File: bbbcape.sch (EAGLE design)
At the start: 30 parts

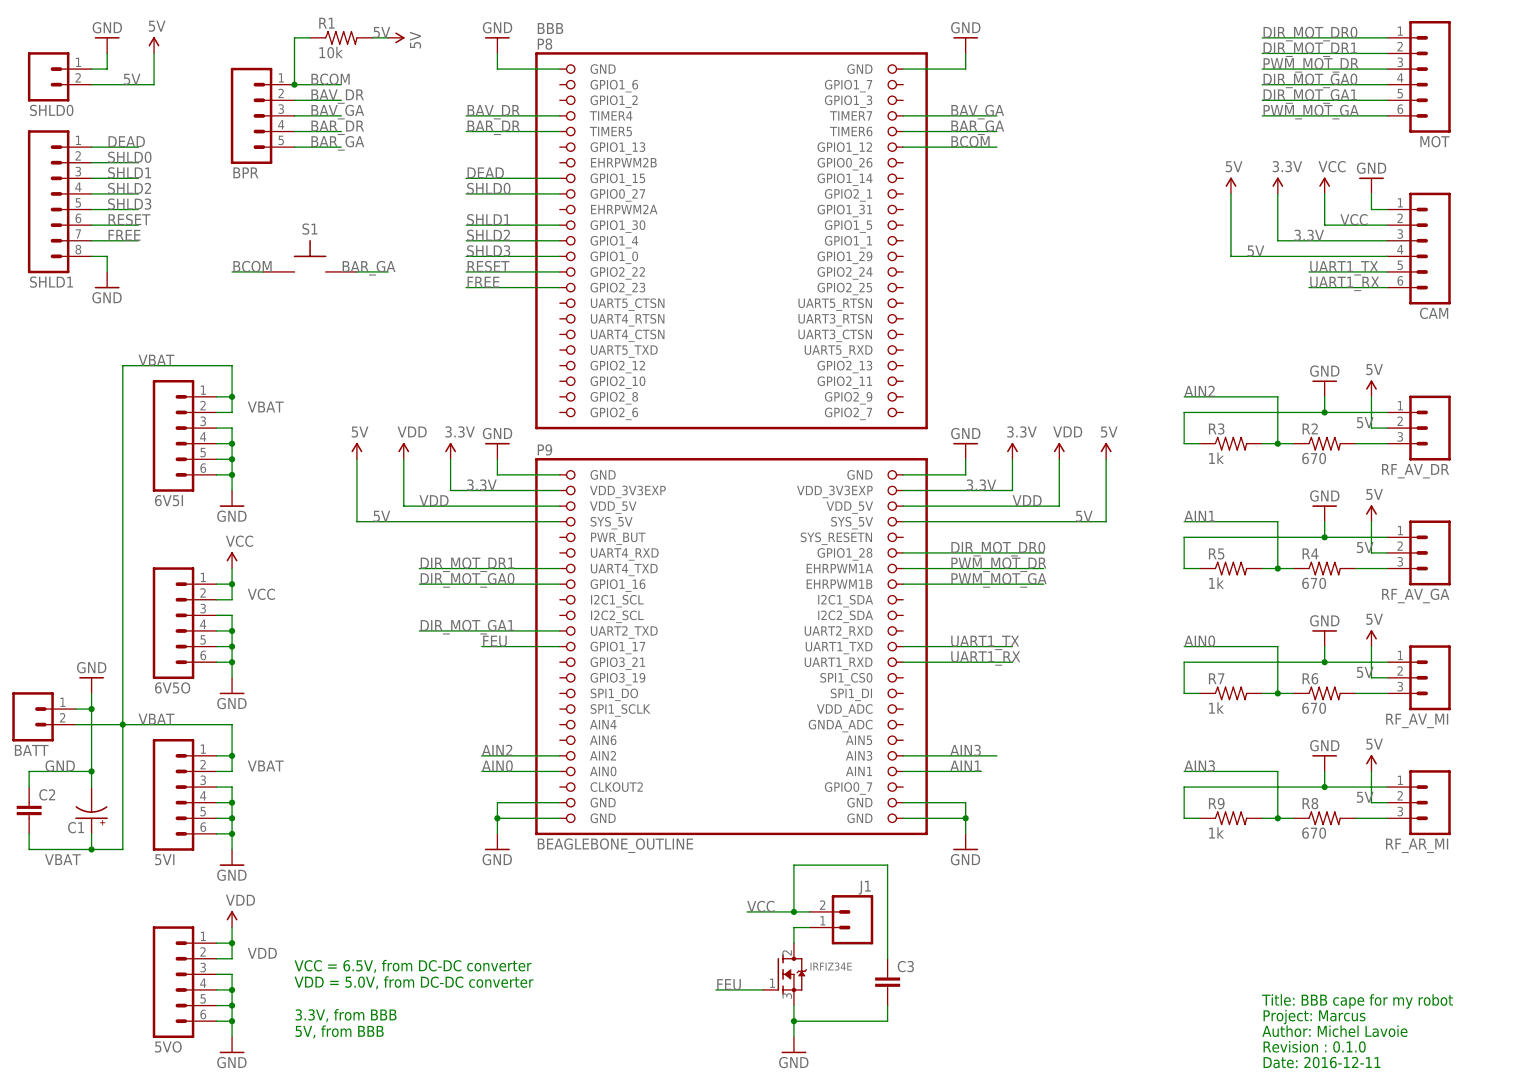
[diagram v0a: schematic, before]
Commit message: Added new DC-DC converter symbol (instead of headers).
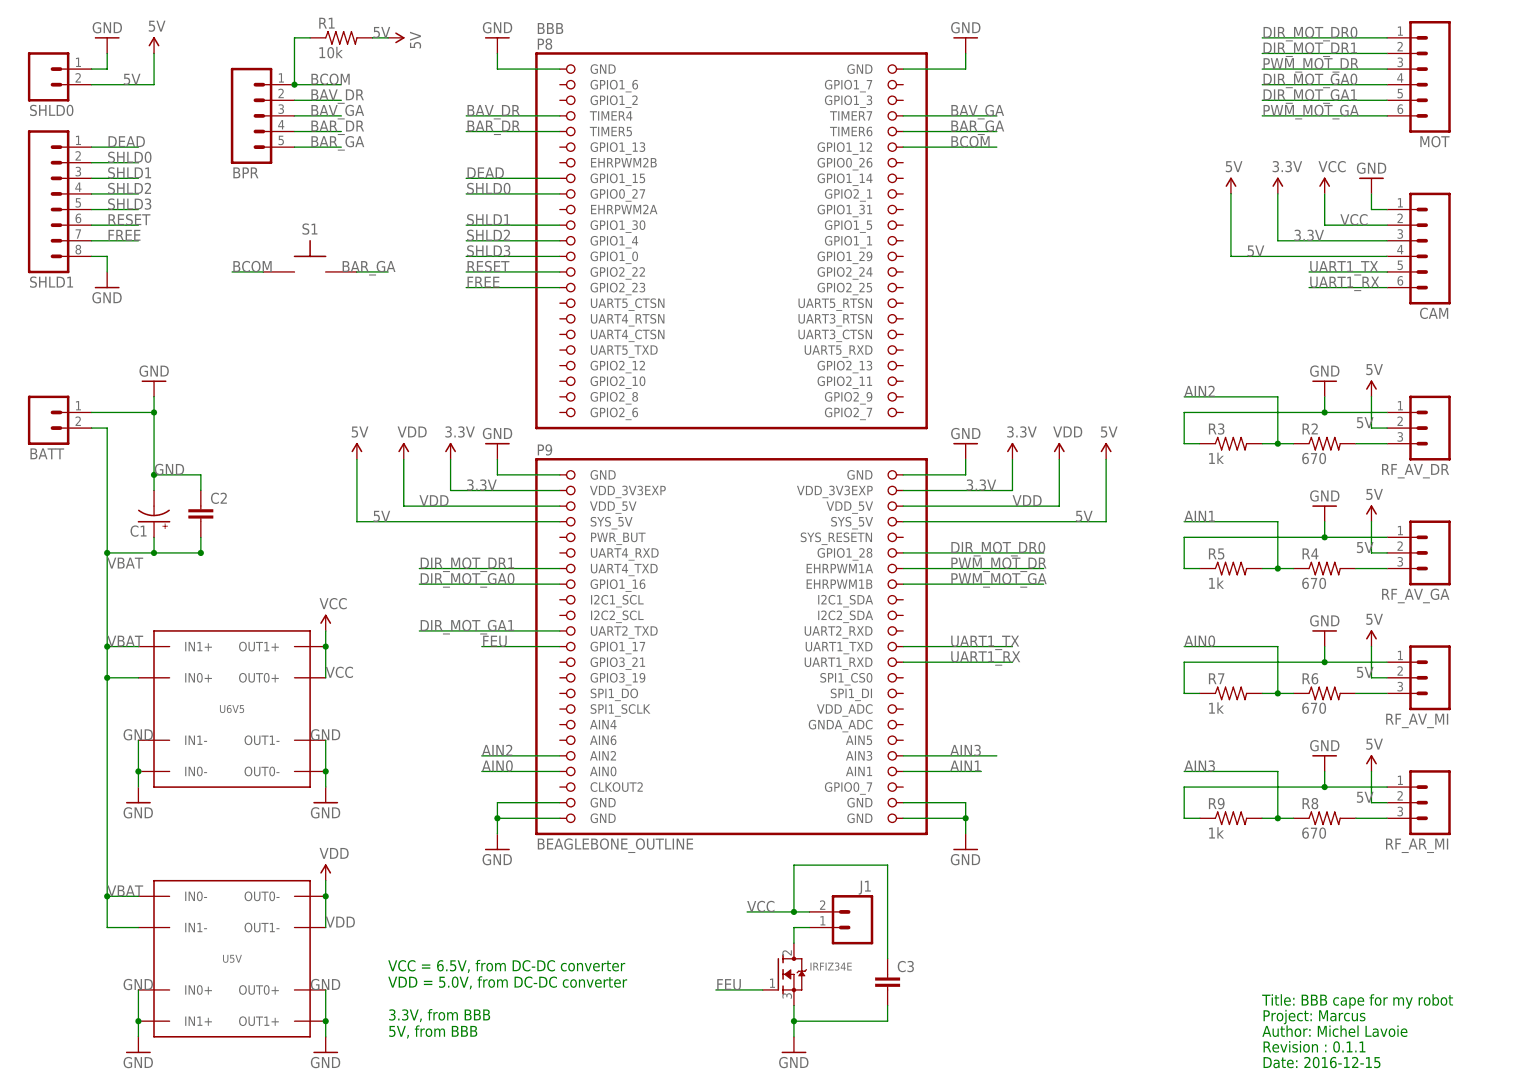
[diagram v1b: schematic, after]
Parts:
- removed 5VI, 5VO, 6V5I, 6V5O: (no value), SparkFun-Connectors:M06SILK_FEMALE_PTH
- added U5V, U6V5: SEEED-MP1584, michel:SEEED-MP1584
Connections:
- net GND: now also U5V.IN0+, U5V.IN1+, U5V.OUT0+, U5V.OUT1+, U6V5.IN0-, U6V5.IN1-, U6V5.OUT0-, U6V5.OUT1-; no longer 5VI.3, 5VI.4, 5VI.5, 5VI.6, 5VO.3, 5VO.4, 5VO.5, 5VO.6, 6V5I.3, 6V5I.4, 6V5I.5, 6V5I.6, 6V5O.3, 6V5O.4, 6V5O.5, 6V5O.6
- net VBAT: now also U5V.IN0-, U5V.IN1-, U6V5.IN0+, U6V5.IN1+; no longer 5VI.1, 5VI.2, 6V5I.1, 6V5I.2
- net VCC: now also U6V5.OUT0+, U6V5.OUT1+; no longer 6V5O.1, 6V5O.2
- net VDD: now also U5V.OUT0-, U5V.OUT1-; no longer 5VO.1, 5VO.2
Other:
- note added: "Date: 2016-12-15"
- note added: "Revision : 0.1.1"
- note removed: "Date: 2016-12-11"
- note removed: "Revision : 0.1.0"
- moved on the sheet: BATT, C1, C2

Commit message: Switched a few pins to confirmed useable pins.
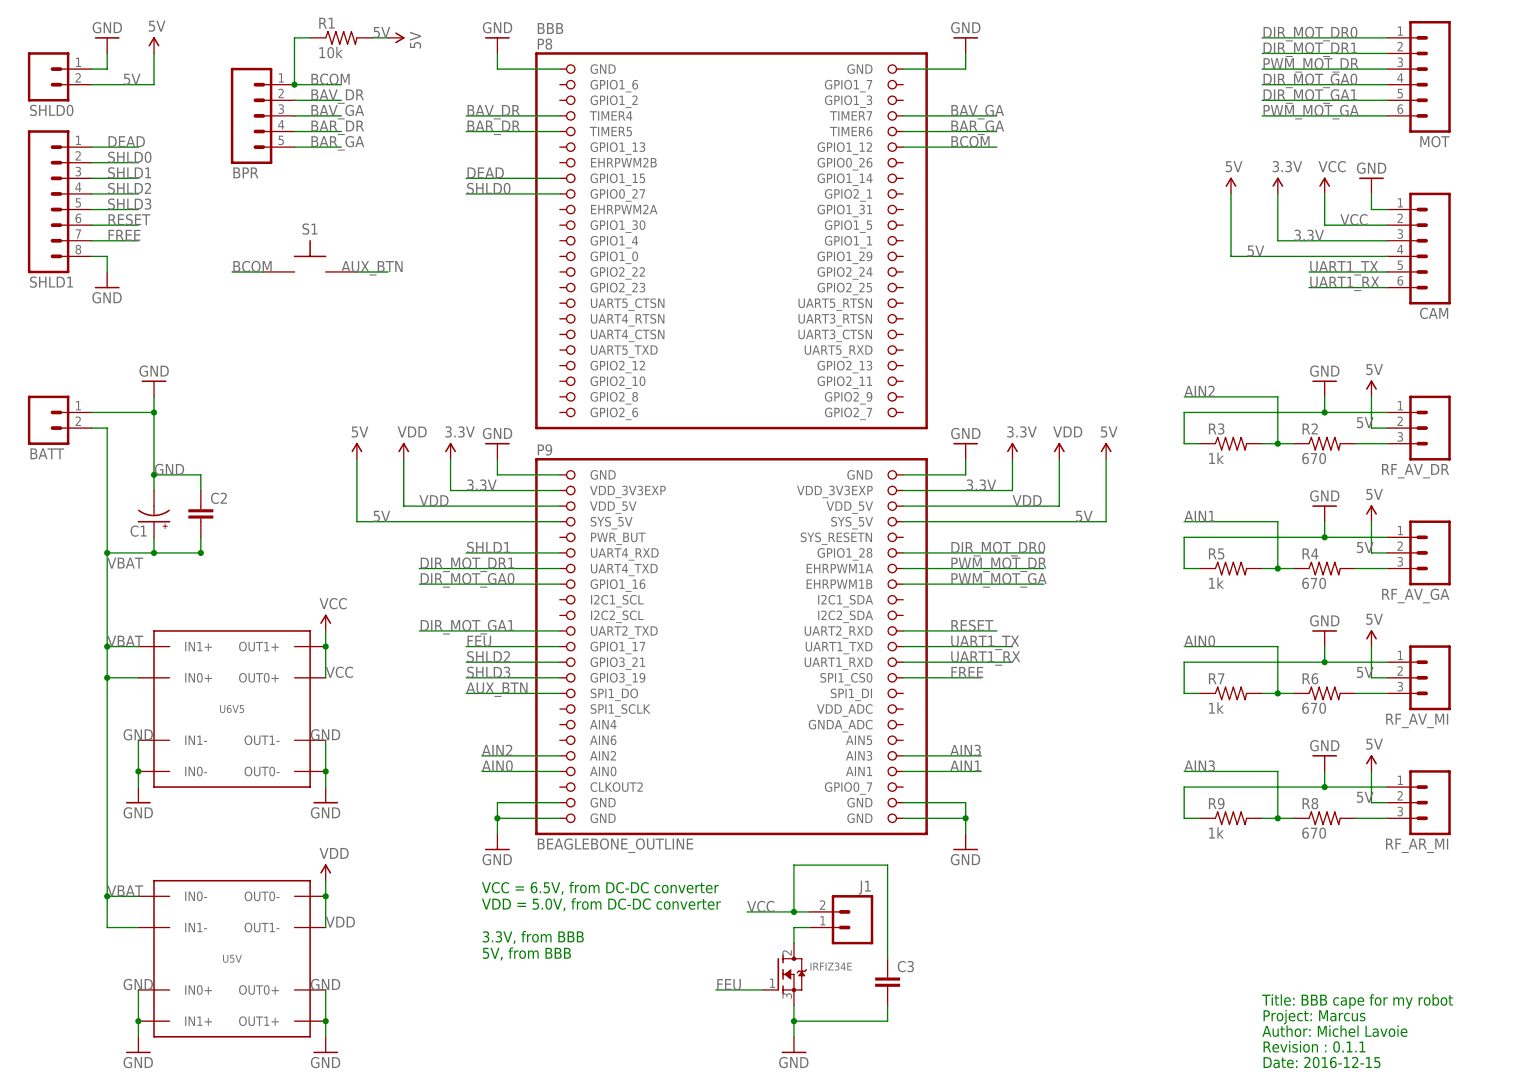
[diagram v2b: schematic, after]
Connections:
- new net AUX_BTN: BBB.SPI1_DO, S1.P$2
- net BAR_GA: no longer S1.P$2
- net FREE: now also BBB.SPI1_CS0; no longer BBB.GPIO2_23
- net RESET: now also BBB.UART2_RXD; no longer BBB.GPIO2_22
- net SHLD1: now also BBB.UART4_RXD; no longer BBB.GPIO1_30
- net SHLD2: now also BBB.GPIO3_21; no longer BBB.GPIO1_4
- net SHLD3: now also BBB.GPIO3_19; no longer BBB.GPIO1_0
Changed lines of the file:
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@@
 <text x="210.82" y="10.16" size="1.778" layer="91">Revision : 0.1.1</text>
 <text x="210.82" y="7.62" size="1.778" layer="91">Date: 2016-12-15</text>
-<text x="68.58" y="12.7" size="1.778" layer="91">VCC = 6.5V, from DC-DC converter
+<text x="83.82" y="25.4" size="1.778" layer="91">VCC = 6.5V, from DC-DC converter
 VDD = 5.0V, from DC-DC converter
 3.3V, from BBB
@@
 </segment>
 <segment>
-<pinref part="BBB" gate="G$1" pin="GPIO1_30"/>
-<wire x1="81.28" y1="144.78" x2="96.52" y2="144.78" width="0.1524" layer="91"/>
-<label x="81.28" y="144.78" size="1.778" layer="95"/>
+<pinref part="BBB" gate="G$1" pin="UART4_RXD"/>
+<wire x1="81.28" y1="91.44" x2="96.52" y2="91.44" width="0.1524" layer="91"/>
+<label x="81.28" y="91.44" size="1.778" layer="95"/>
 </segment>
 </net>
@@
 </segment>
 <segment>
-<pinref part="BBB" gate="G$1" pin="GPIO1_4"/>
-<wire x1="81.28" y1="142.24" x2="96.52" y2="142.24" width="0.1524" layer="91"/>
-<label x="81.28" y="142.24" size="1.778" layer="95"/>
+<pinref part="BBB" gate="G$1" pin="GPIO3_21"/>
+<wire x1="81.28" y1="73.66" x2="96.52" y2="73.66" width="0.1524" layer="91"/>
+<label x="81.28" y="73.66" size="1.778" layer="95"/>
 </segment>
 </net>
@@
 </segment>
 <segment>
-<pinref part="BBB" gate="G$1" pin="GPIO1_0"/>
-<wire x1="81.28" y1="139.7" x2="96.52" y2="139.7" width="0.1524" layer="91"/>
-<label x="81.28" y="139.7" size="1.778" layer="95"/>
+<pinref part="BBB" gate="G$1" pin="GPIO3_19"/>
+<wire x1="81.28" y1="71.12" x2="96.52" y2="71.12" width="0.1524" layer="91"/>
+<label x="81.28" y="71.12" size="1.778" layer="95"/>
 </segment>
 </net>
@@
 </segment>
 <segment>
-<pinref part="BBB" gate="G$1" pin="GPIO2_22"/>
-<wire x1="81.28" y1="137.16" x2="96.52" y2="137.16" width="0.1524" layer="91"/>
-<label x="81.28" y="137.16" size="1.778" layer="95"/>
+<pinref part="BBB" gate="G$1" pin="UART2_RXD"/>
+<wire x1="167.64" y1="78.74" x2="152.4" y2="78.74" width="0.1524" layer="91"/>
+<label x="160.02" y="78.74" size="1.778" layer="95"/>
 </segment>
 </net>
@@
 </segment>
 <segment>
-<pinref part="BBB" gate="G$1" pin="GPIO2_23"/>
-<wire x1="81.28" y1="134.62" x2="96.52" y2="134.62" width="0.1524" layer="91"/>
-<label x="81.28" y="134.62" size="1.778" layer="95"/>
+<pinref part="BBB" gate="G$1" pin="SPI1_CS0"/>
+<wire x1="165.1" y1="71.12" x2="152.4" y2="71.12" width="0.1524" layer="91"/>
+<label x="160.02" y="71.12" size="1.778" layer="95"/>
 </segment>
 </net>
@@
 <wire x1="167.64" y1="160.02" x2="152.4" y2="160.02" width="0.1524" layer="91"/>
 <label x="160.02" y="160.02" size="1.778" layer="95"/>
-</segment>
-<segment>
-<wire x1="68.58" y1="137.16" x2="63.5" y2="137.16" width="0.1524" layer="91"/>
-<label x="60.96" y="137.16" size="1.778" layer="95"/>
-<pinref part="S1" gate="G$1" pin="P$2"/>
 </segment>
 </net>
@@
 <segment>
 <pinref part="BBB" gate="G$1" pin="AIN3"/>
-<wire x1="167.64" y1="58.42" x2="152.4" y2="58.42" width="0.1524" layer="91"/>
+<wire x1="165.1" y1="58.42" x2="152.4" y2="58.42" width="0.1524" layer="91"/>
 <label x="160.02" y="58.42" size="1.778" layer="95"/>
 </segment>
@@
 <segment>
 <pinref part="BBB" gate="G$1" pin="GPIO1_17"/>
-<wire x1="83.82" y1="76.2" x2="96.52" y2="76.2" width="0.1524" layer="91"/>
-<label x="83.82" y="76.2" size="1.778" layer="95"/>
+<wire x1="81.28" y1="76.2" x2="96.52" y2="76.2" width="0.1524" layer="91"/>
+<label x="81.28" y="76.2" size="1.778" layer="95"/>
 </segment>
 <segment>
@@
 </segment>
 </net>
+<net name="AUX_BTN" class="0">
+<segment>
+<pinref part="BBB" gate="G$1" pin="SPI1_DO"/>
+<wire x1="81.28" y1="68.58" x2="96.52" y2="68.58" width="0.1524" layer="91"/>
+<label x="81.28" y="68.58" size="1.778" layer="95"/>
+</segment>
+<segment>
+<wire x1="68.58" y1="137.16" x2="63.5" y2="137.16" width="0.1524" layer="91"/>
+<label x="60.96" y="137.16" size="1.778" layer="95"/>
+<pinref part="S1" gate="G$1" pin="P$2"/>
+</segment>
+</net>

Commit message: PCB done.
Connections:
- removed net N$6: R8.2
- new net N$2: R4.2, RF_AV_GA.3
- net 5V: now also RF_AR_MI.2, RF_AV_GA.2, RF_AV_MI.2
- net GND: now also RF_AR_MI.1, RF_AV_GA.1, RF_AV_MI.1
- net N$4: now also R6.2, RF_AV_MI.3; no longer R4.2
- net N$5: now also R8.2, RF_AR_MI.3; no longer R6.2
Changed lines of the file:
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@@
 <setting verticaltext="up"/>
 </settings>
-<grid distance="0.1" unitdist="inch" unit="inch" style="dots" multiple="1" display="yes" altdistance="0.01" altunitdist="inch" altunit="inch"/>
+<grid distance="0.1" unitdist="inch" unit="inch" style="lines" multiple="1" display="no" altdistance="0.01" altunitdist="inch" altunit="inch"/>
 <layers>
 <layer number="1" name="Top" color="4" fill="1" visible="no" active="no"/>
@@
 <instance part="R3" gate="G$1" x="205.74" y="109.22"/>
 <instance part="GND14" gate="1" x="220.98" y="119.38" rot="R180"/>
-<instance part="SUPPLY10" gate="G$1" x="228.6" y="116.84"/>
+<instance part="SUPPLY10" gate="G$1" x="228.6" y="111.76" rot="R90"/>
 <instance part="R4" gate="G$1" x="220.98" y="88.9"/>
 <instance part="R5" gate="G$1" x="205.74" y="88.9"/>
 <instance part="GND15" gate="1" x="220.98" y="99.06" rot="R180"/>
-<instance part="SUPPLY11" gate="G$1" x="228.6" y="96.52"/>
+<instance part="SUPPLY11" gate="G$1" x="228.6" y="91.44" rot="R90"/>
 <instance part="R6" gate="G$1" x="220.98" y="68.58"/>
 <instance part="R7" gate="G$1" x="205.74" y="68.58"/>
 <instance part="GND16" gate="1" x="220.98" y="78.74" rot="R180"/>
-<instance part="SUPPLY12" gate="G$1" x="228.6" y="76.2"/>
+<instance part="SUPPLY12" gate="G$1" x="228.6" y="71.12" rot="R90"/>
 <instance part="R8" gate="G$1" x="220.98" y="48.26"/>
 <instance part="R9" gate="G$1" x="205.74" y="48.26"/>
 <instance part="GND17" gate="1" x="220.98" y="58.42" rot="R180"/>
-<instance part="SUPPLY13" gate="G$1" x="228.6" y="55.88"/>
+<instance part="SUPPLY13" gate="G$1" x="228.6" y="50.8" rot="R90"/>
 <instance part="SUPPLY14" gate="VDD" x="71.12" y="106.68"/>
 <instance part="SUPPLY1" gate="VDD" x="58.42" y="38.1"/>
@@
 <wire x1="198.12" y1="88.9" x2="198.12" y2="93.98" width="0.1524" layer="91"/>
 <wire x1="198.12" y1="93.98" x2="220.98" y2="93.98" width="0.1524" layer="91"/>
+<pinref part="RF_AV_GA" gate="J$1" pin="1"/>
 <wire x1="220.98" y1="93.98" x2="231.14" y2="93.98" width="0.1524" layer="91"/>
 <junction x="220.98" y="93.98"/>
@@
 <wire x1="198.12" y1="68.58" x2="198.12" y2="73.66" width="0.1524" layer="91"/>
 <wire x1="198.12" y1="73.66" x2="220.98" y2="73.66" width="0.1524" layer="91"/>
+<pinref part="RF_AV_MI" gate="J$1" pin="1"/>
 <wire x1="220.98" y1="73.66" x2="231.14" y2="73.66" width="0.1524" layer="91"/>
 <junction x="220.98" y="73.66"/>
@@
 <wire x1="198.12" y1="48.26" x2="198.12" y2="53.34" width="0.1524" layer="91"/>
 <wire x1="198.12" y1="53.34" x2="220.98" y2="53.34" width="0.1524" layer="91"/>
+<pinref part="RF_AR_MI" gate="J$1" pin="1"/>
 <wire x1="220.98" y1="53.34" x2="231.14" y2="53.34" width="0.1524" layer="91"/>
 <junction x="220.98" y="53.34"/>
@@
 <segment>
 <pinref part="SUPPLY10" gate="G$1" pin="5V"/>
-<wire x1="228.6" y1="116.84" x2="228.6" y2="111.76" width="0.1524" layer="91"/>
 <pinref part="RF_AV_DR" gate="J$1" pin="2"/>
 <wire x1="228.6" y1="111.76" x2="231.14" y2="111.76" width="0.1524" layer="91"/>
-<label x="226.06" y="111.76" size="1.778" layer="95"/>
 </segment>
 <segment>
 <pinref part="SUPPLY11" gate="G$1" pin="5V"/>
-<wire x1="228.6" y1="96.52" x2="228.6" y2="91.44" width="0.1524" layer="91"/>
+<pinref part="RF_AV_GA" gate="J$1" pin="2"/>
 <wire x1="228.6" y1="91.44" x2="231.14" y2="91.44" width="0.1524" layer="91"/>
-<label x="226.06" y="91.44" size="1.778" layer="95"/>
 </segment>
 <segment>
 <pinref part="SUPPLY12" gate="G$1" pin="5V"/>
-<wire x1="228.6" y1="76.2" x2="228.6" y2="71.12" width="0.1524" layer="91"/>
+<pinref part="RF_AV_MI" gate="J$1" pin="2"/>
 <wire x1="228.6" y1="71.12" x2="231.14" y2="71.12" width="0.1524" layer="91"/>
-<label x="226.06" y="71.12" size="1.778" layer="95"/>
 </segment>
 <segment>
 <pinref part="SUPPLY13" gate="G$1" pin="5V"/>
-<wire x1="228.6" y1="55.88" x2="228.6" y2="50.8" width="0.1524" layer="91"/>
+<pinref part="RF_AR_MI" gate="J$1" pin="2"/>
 <wire x1="228.6" y1="50.8" x2="231.14" y2="50.8" width="0.1524" layer="91"/>
-<label x="226.06" y="50.8" size="1.778" layer="95"/>
 </segment>
 </net>
@@
 </segment>
 </net>
-<net name="N$2" class="0">
-<segment>
-<pinref part="R2" gate="G$1" pin="2"/>
-<pinref part="RF_AV_DR" gate="J$1" pin="3"/>
-<wire x1="226.06" y1="109.22" x2="231.14" y2="109.22" width="0.1524" layer="91"/>
-</segment>
-</net>
-<net name="N$4" class="0">
-<segment>
-<pinref part="R4" gate="G$1" pin="2"/>
-<wire x1="226.06" y1="88.9" x2="231.14" y2="88.9" width="0.1524" layer="91"/>
-</segment>
-</net>
-<net name="N$5" class="0">
-<segment>
-<pinref part="R6" gate="G$1" pin="2"/>
-<wire x1="226.06" y1="68.58" x2="231.14" y2="68.58" width="0.1524" layer="91"/>
-</segment>
-</net>
-<net name="N$6" class="0">
-<segment>
-<pinref part="R8" gate="G$1" pin="2"/>
-<wire x1="226.06" y1="48.26" x2="231.14" y2="48.26" width="0.1524" layer="91"/>
-</segment>
-</net>
 <net name="AIN2" class="0">
 <segment>
@@
 </segment>
 </net>
+<net name="N$1" class="0">
+<segment>
+<pinref part="R2" gate="G$1" pin="2"/>
+<pinref part="RF_AV_DR" gate="J$1" pin="3"/>
+<wire x1="226.06" y1="109.22" x2="231.14" y2="109.22" width="0.1524" layer="91"/>
+</segment>
+</net>
+<net name="N$2" class="0">
+<segment>
+<pinref part="R4" gate="G$1" pin="2"/>
+<pinref part="RF_AV_GA" gate="J$1" pin="3"/>
+<wire x1="226.06" y1="88.9" x2="231.14" y2="88.9" width="0.1524" layer="91"/>
+</segment>
+</net>
+<net name="N$4" class="0">
+<segment>
+<pinref part="R6" gate="G$1" pin="2"/>
+<pinref part="RF_AV_MI" gate="J$1" pin="3"/>
+<wire x1="226.06" y1="68.58" x2="231.14" y2="68.58" width="0.1524" layer="91"/>
+</segment>
+</net>
+<net name="N$5" class="0">
+<segment>
+<pinref part="R8" gate="G$1" pin="2"/>
+<pinref part="RF_AR_MI" gate="J$1" pin="3"/>
+<wire x1="226.06" y1="48.26" x2="231.14" y2="48.26" width="0.1524" layer="91"/>
+</segment>
+</net>
 </nets>
 </sheet>
 </sheets>
+<errors>
+</errors>
 </schematic>
 </drawing>
